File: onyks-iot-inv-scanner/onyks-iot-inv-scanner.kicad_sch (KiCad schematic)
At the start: 21 parts, among them J1 Conn_01x24_MountingPin, J2 USB_C_Receptacle, J3 Conn_01x04, SW1 EN, SW2 BOOT, U2 ESP32-S3-WROOM-1

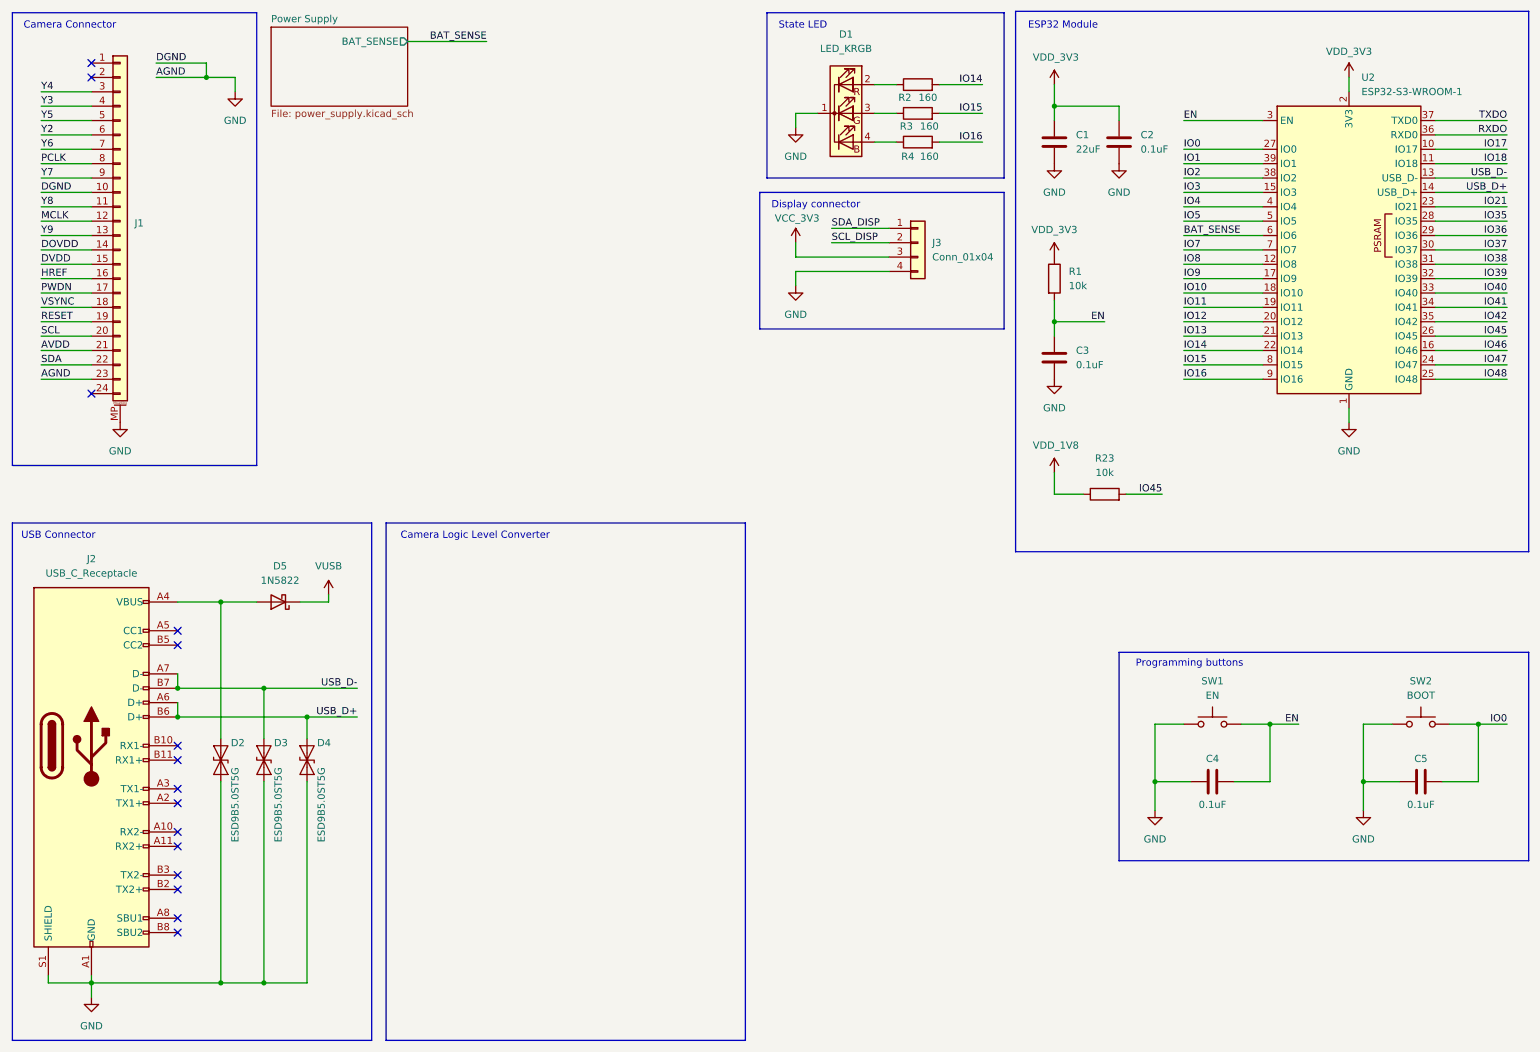
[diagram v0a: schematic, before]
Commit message: moved camera to separate schematic and added llc's for it
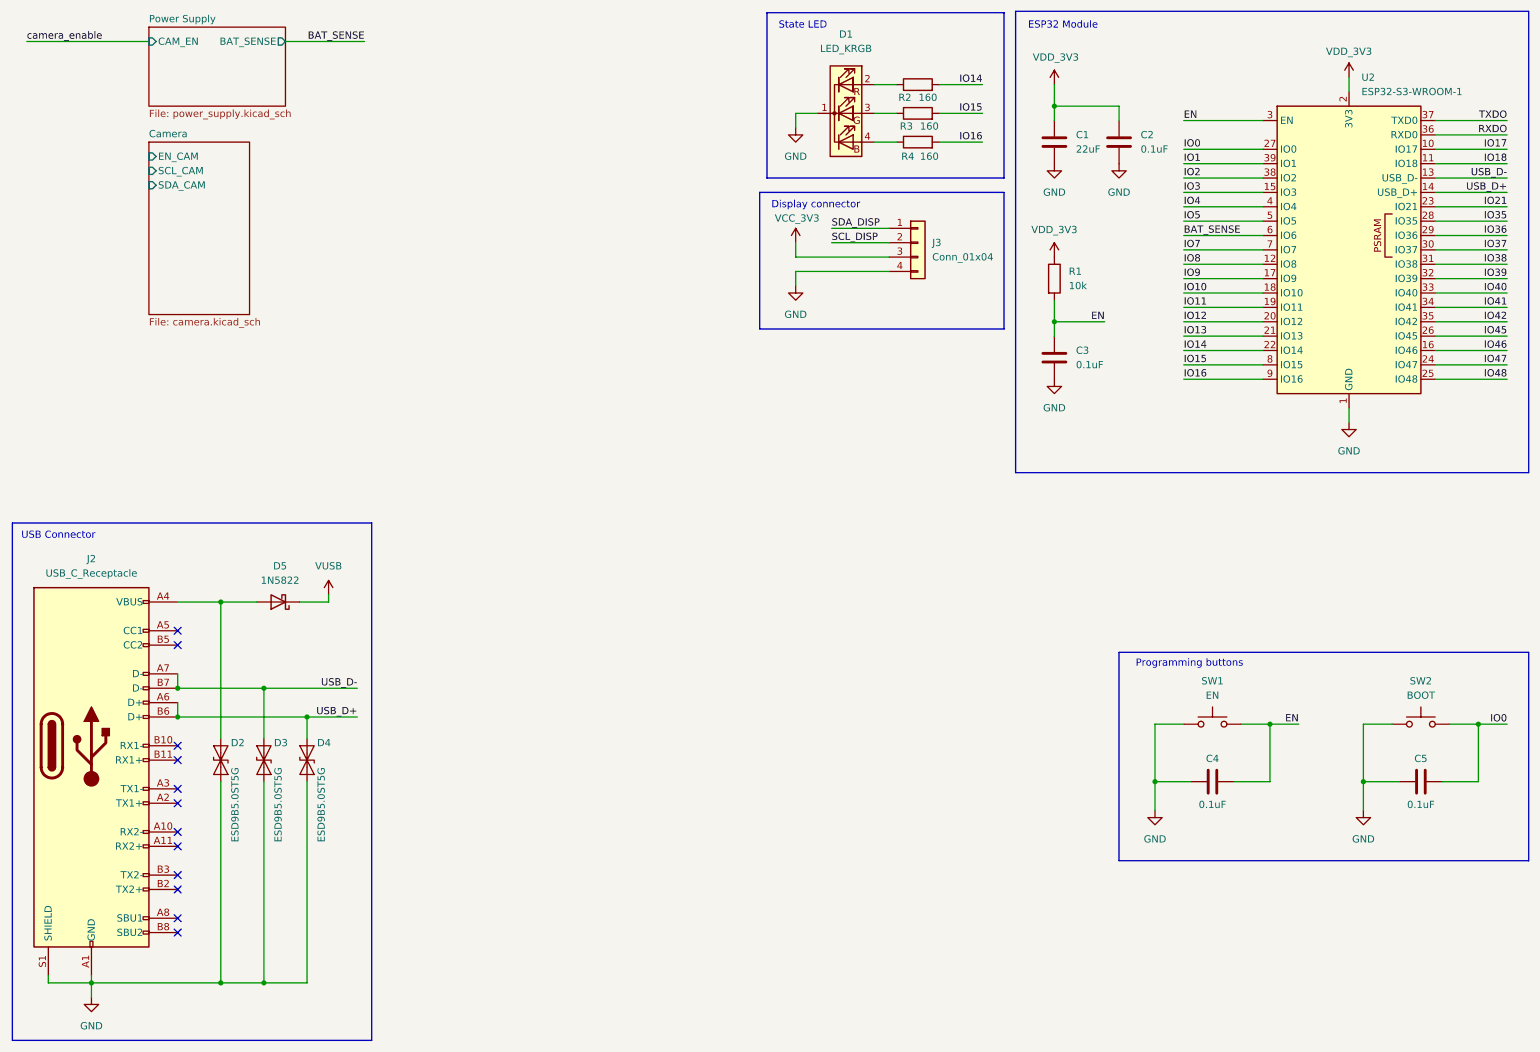
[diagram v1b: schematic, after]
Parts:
- removed J1: Conn_01x24_MountingPin, Connector_FFC-FPC:Molex_502244-2430_1x24-1MP_P0.5mm_Horizontal, symbol Connector_Generic_MountingPin:Conn_01x24_MountingPin
- removed R23: 10k, symbol Device:R
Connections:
- no-connect marks 15 -> 12
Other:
- added sheet Camera (camera.kicad_sch)
- sheet Power Supply ports: added CAM_EN; removed none
- note removed: "Camera Connector"
- note removed: "Camera Logic Level Converter"

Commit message: added trigger button and connected cammera with llc and power supply
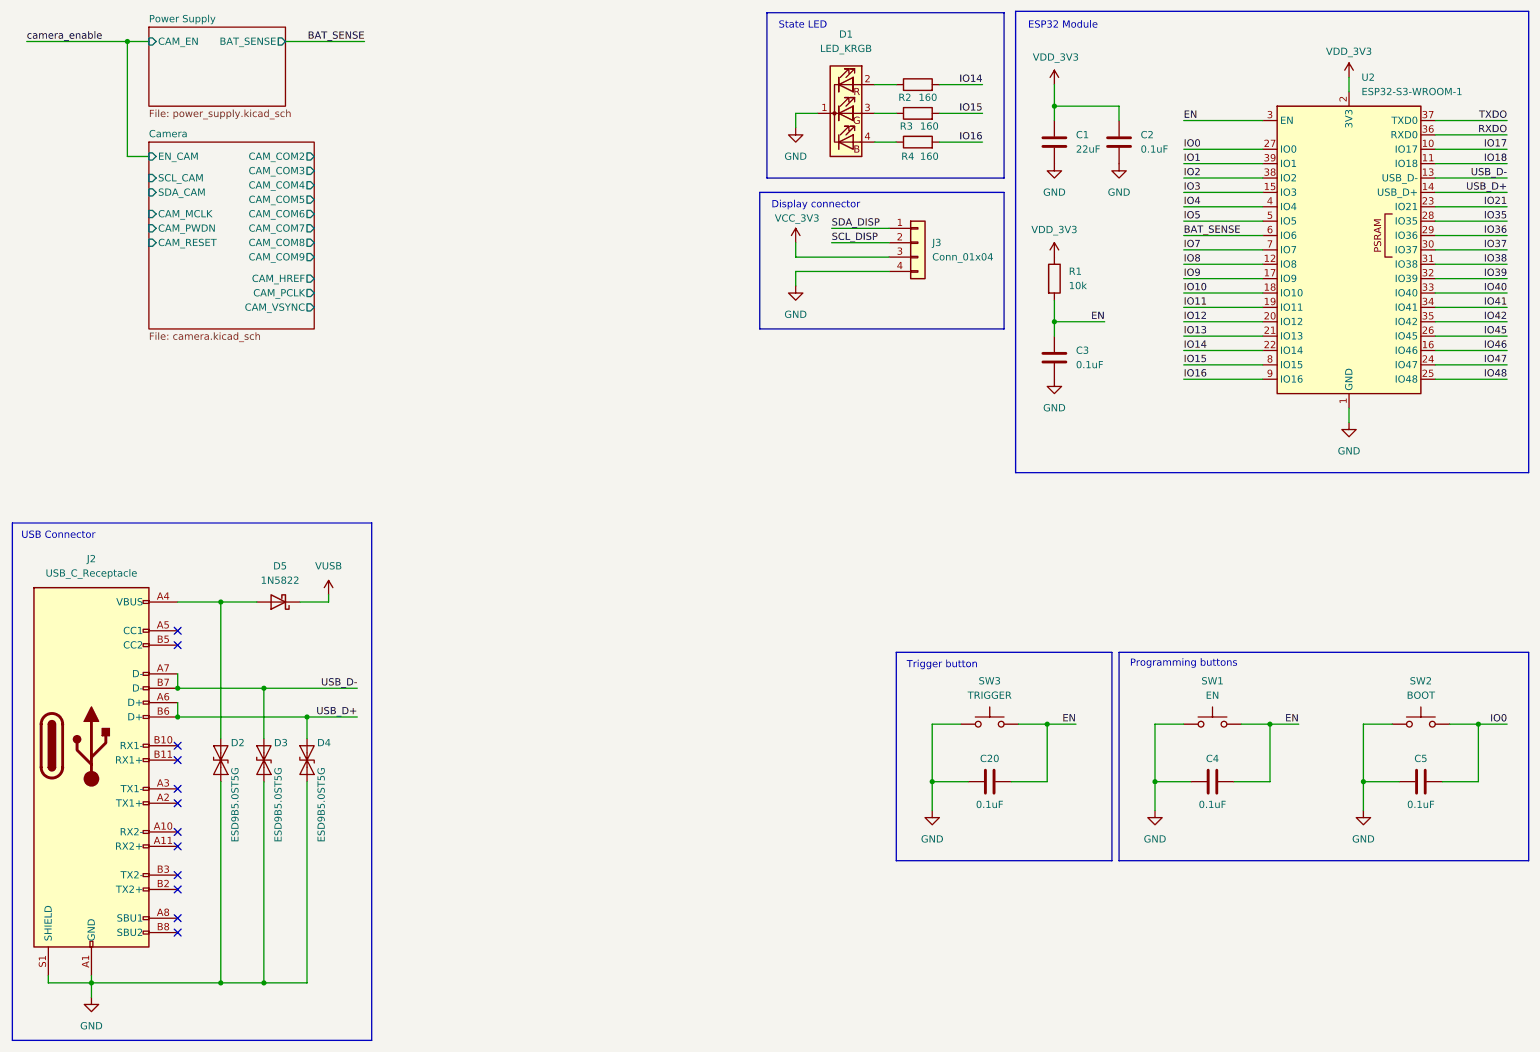
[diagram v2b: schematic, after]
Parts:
- added C20: 0.1uF, symbol Device:C
- added SW3: TRIGGER, symbol Switch:SW_Push
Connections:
- net EN: now also C20.2, SW3.2
- net GND: now also C20.1, SW3.1
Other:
- sheet Camera ports: added CAM_COM2, CAM_COM3, CAM_COM4, CAM_COM5, CAM_COM6, CAM_COM7, CAM_COM8, CAM_COM9, CAM_HREF, CAM_MCLK, CAM_PCLK, CAM_PWDN, CAM_RESET, CAM_VSYNC; removed none
- note added: "Trigger button"

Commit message: allegedly connected external devices for gpio
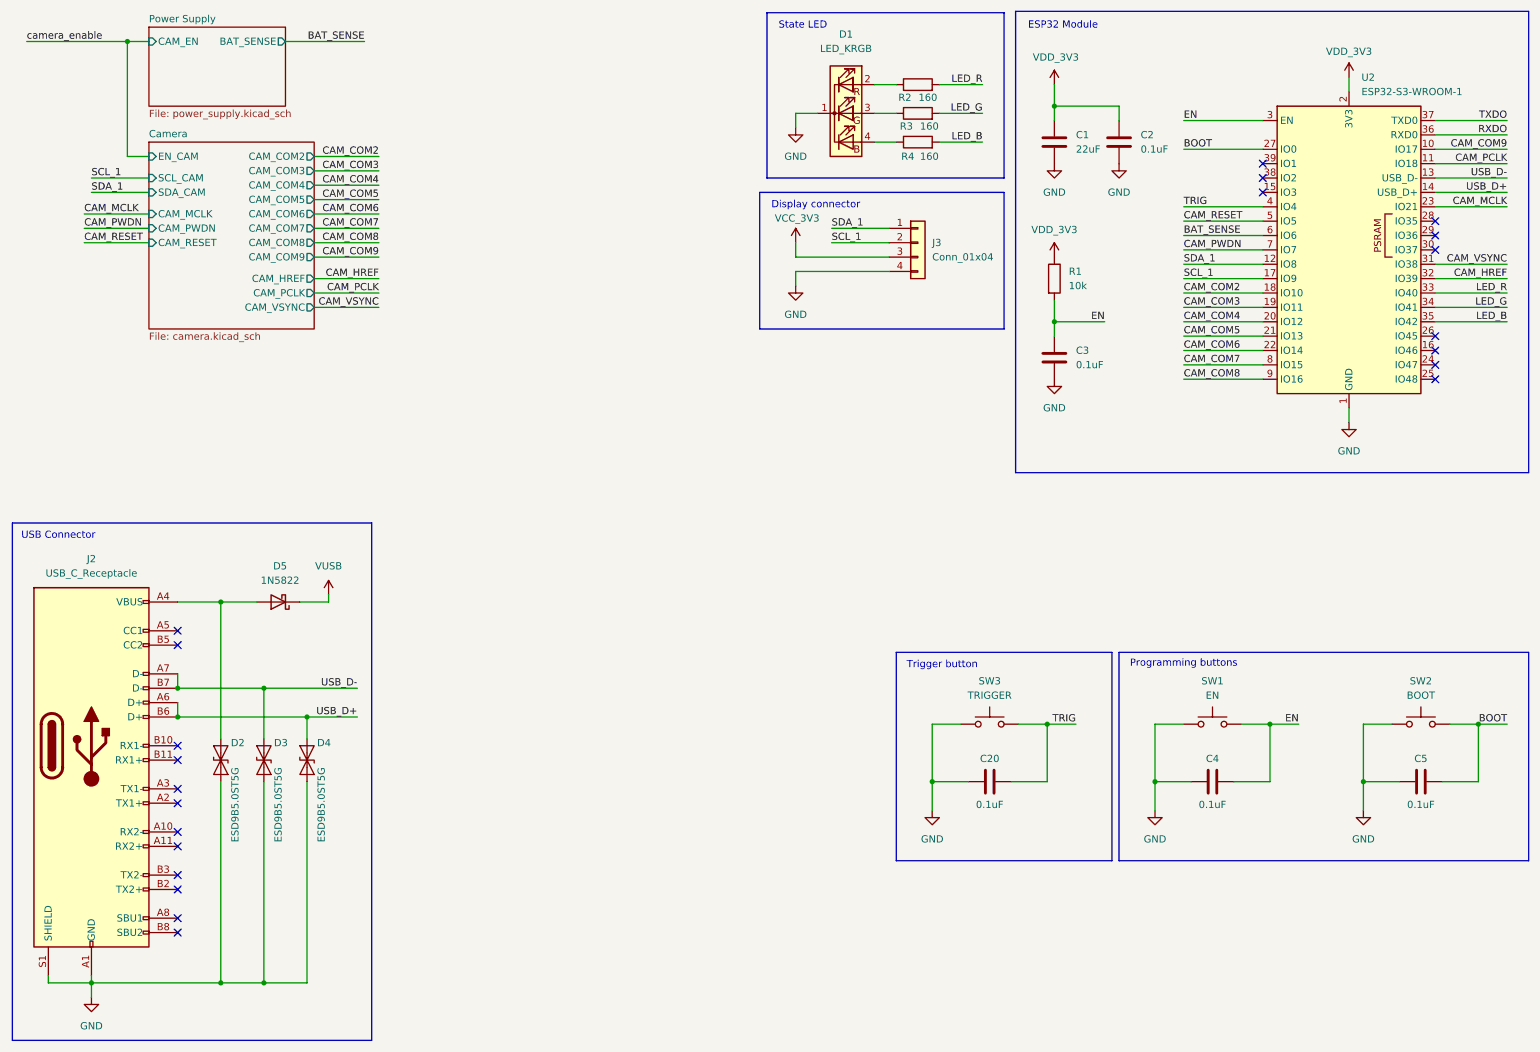
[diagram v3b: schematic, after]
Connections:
- net SCL_DISP is gone; now on net SCL_1: J3.2 (Pin_2)
- net SDA_DISP is gone; now on net SDA_1: J3.1 (Pin_1)
- net EN: no longer C20.2, SW3.2
- net IO0 renamed BOOT
- net IO1: no longer names the net of U2.39 (IO1)
- net IO10 renamed CAM_COM2
- net IO11 renamed CAM_COM3
- net IO12 renamed CAM_COM4
- net IO13 renamed CAM_COM5
- net IO14 renamed CAM_COM6
- net CAM_COM6: no longer R2.2
- net IO15 renamed CAM_COM7
- net CAM_COM7: no longer R3.2
- net IO16 renamed CAM_COM8
- net CAM_COM8: no longer R4.2
- net IO17 renamed CAM_COM9
- net IO18 renamed CAM_PCLK
- net IO2: no longer names the net of U2.38 (IO2)
- net IO21 renamed CAM_MCLK
- net IO3: no longer names the net of U2.15 (IO3)
- net IO35: no longer names the net of U2.28 (IO35)
- net IO36: no longer names the net of U2.29 (IO36)
- net IO37: no longer names the net of U2.30 (IO37)
- net IO38 renamed CAM_VSYNC
- net IO39 renamed CAM_HREF
- net IO4 renamed TRIG
- net TRIG: now also C20.2, SW3.2
- net IO40 renamed LED_R
- net LED_R: now also R2.2
- net IO41 renamed LED_G
- net LED_G: now also R3.2
- net IO42 renamed LED_B
- net LED_B: now also R4.2
- net IO45: no longer names the net of U2.26 (IO45)
- net IO46: no longer names the net of U2.16 (IO46)
- net IO47: no longer names the net of U2.24 (IO47)
- net IO48: no longer names the net of U2.25 (IO48)
- net IO5 renamed CAM_RESET
- net IO7 renamed CAM_PWDN
- net IO8 renamed SDA_1
- net IO9 renamed SCL_1
- no-connect marks 12 -> 22

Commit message: connected enable pin for camera to gpio
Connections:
- net camera_enable: now also U2.15 (IO3)
- no-connect marks 22 -> 21
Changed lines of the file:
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@@
-	)
-	(no_connect
-		(at 234.95 45.72)
 	)
 	(no_connect
@@
 		(pts
 			(xy 220.98 50.8) (xy 234.95 50.8)
+		)
+		(stroke
+			(width 0)
+			(type default)
+		)
+	)
+	(wire
+		(pts
+			(xy 220.98 45.72) (xy 234.95 45.72)
 		)
 		(stroke
@@
 		)
 	)
+	(label "camera_enable"
+		(at 220.98 45.72 0)
+		(effects
+			(font
+				(size 1.27 1.27)
+			)
+			(justify left bottom)
+		)
+	)

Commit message: changed en pin because of strapping pin function of previous
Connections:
- net camera_enable: now also U2.38 (IO2); no longer U2.15 (IO3)
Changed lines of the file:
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@@
-	)
-	(no_connect
-		(at 234.95 43.18)
 	)
 	(no_connect
@@
 	)
 	(no_connect
+		(at 234.95 45.72)
+	)
+	(no_connect
 		(at 265.43 78.74)
 	)
@@
 	(wire
 		(pts
-			(xy 220.98 45.72) (xy 234.95 45.72)
+			(xy 220.98 43.18) (xy 234.95 43.18)
 		)
 		(stroke
@@
 	)
 	(label "camera_enable"
-		(at 220.98 45.72 0)
-		(effects
-			(font
+		(at 220.98 43.18 0)
+		(effects
+			(font

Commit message: moved href pin because of pull-up default function of previous pin
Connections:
- net CAM_HREF: now also U2.24 (IO47); no longer U2.32 (IO39)
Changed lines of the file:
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@@
-	)
-	(no_connect
-		(at 265.43 76.2)
 	)
 	(no_connect
@@
 	)
 	(no_connect
+		(at 265.43 60.96)
+	)
+	(no_connect
 		(at 43.18 153.67)
 	)
@@
 	(wire
 		(pts
-			(xy 265.43 60.96) (xy 278.13 60.96)
-		)
-		(stroke
-			(width 0)
-			(type default)
-		)
-	)
-	(wire
-		(pts
 			(xy 252.73 139.7) (xy 252.73 149.86)
 		)
@@
 		(pts
 			(xy 26.67 49.53) (xy 38.1 49.53)
+		)
+		(stroke
+			(width 0)
+			(type default)
+		)
+	)
+	(wire
+		(pts
+			(xy 265.43 76.2) (xy 278.13 76.2)
 		)
 		(stroke
@@
 		)
 	)
+	(label "CAM_HREF"
+		(at 278.13 76.2 180)
+		(effects
+			(font
+				(size 1.27 1.27)
+			)
+			(justify right bottom)
+		)
+	)
 	(label "CAM_RESET"
 		(at 220.98 50.8 0)
@@
 		(effects
 			(font
-				(size 1.27 1.27)
-			)
-			(justify right bottom)
-		)
-	)
-	(label "CAM_HREF"
-		(at 278.13 60.96 180)
-		(effects
-			(font

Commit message: unpin usb data lines from battery management IC, becouse of possibly jamming signal
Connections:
- net INT_N: now reaches U2.25 (IO48)
- net BAT_SENSE renamed CE_N
- no-connect marks 21 -> 22
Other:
- sheet Power Supply ports: added CE_N, D+, D-, INT_N, SCL, SDA; removed BAT_SENSE
